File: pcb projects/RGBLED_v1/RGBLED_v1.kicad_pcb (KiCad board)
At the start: 2 copper layers, 63 x 43 mm, 26 parts, among them CN1 USB_B_Micro, CN2 Conn_01x03_Pin, J1 Conn_02x02_Odd_Even, SW1 SW_MEC_5E, U1 STM32F091RBTx, U3 LM1117T-3.3, Y1 32.768kHz

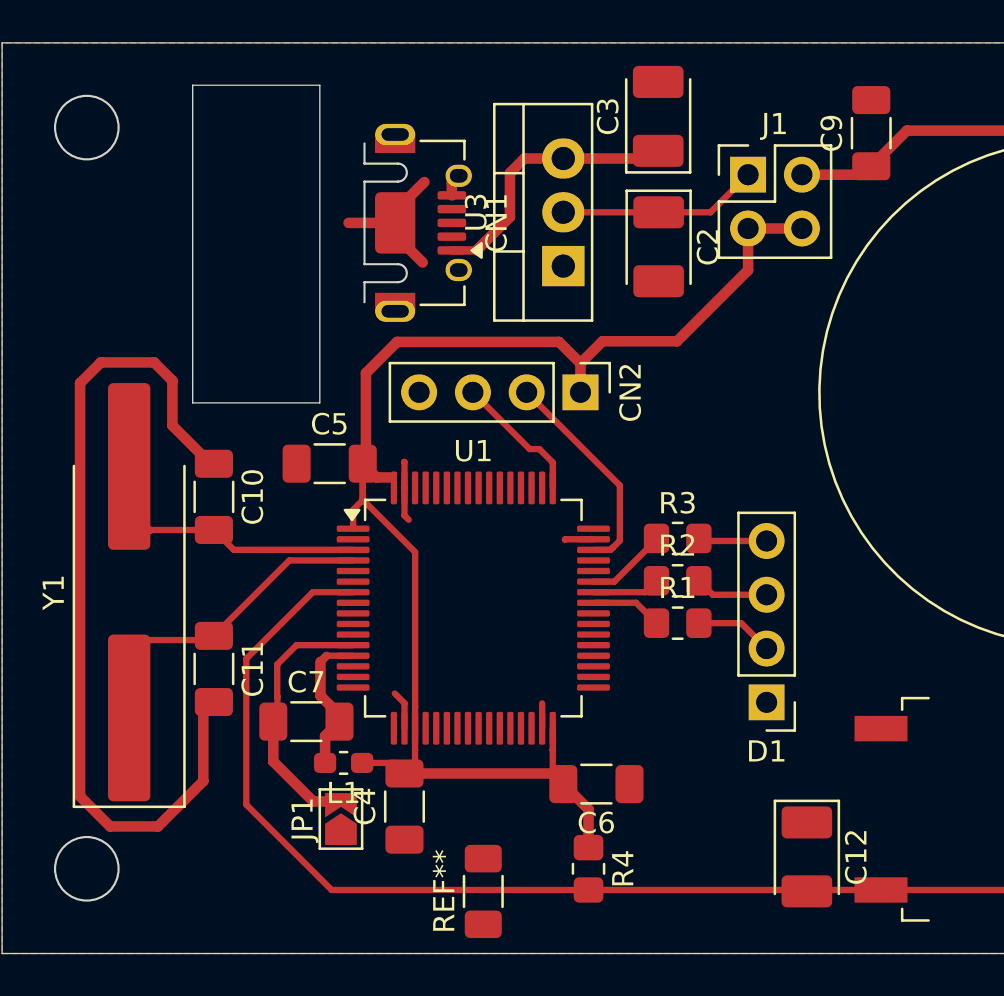
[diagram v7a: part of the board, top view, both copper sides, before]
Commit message: D1 sch fix, stab fix, gnd zone fixed, started verification and BOM
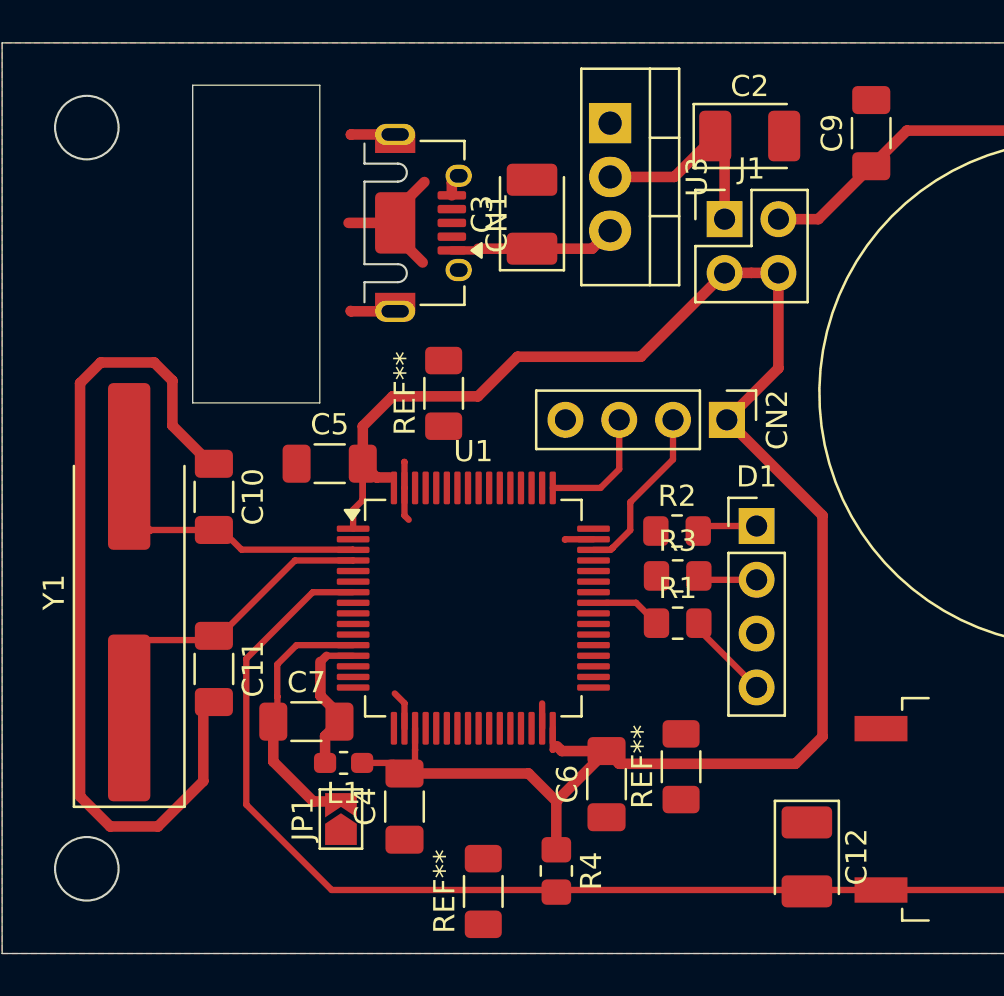
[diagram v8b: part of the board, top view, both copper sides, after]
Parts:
- added REF**: R_1206_3216Metric_Pad1.30x1.75mm_HandSolder, Resistor_SMD:R_1206_3216Metric_Pad1.30x1.75mm_HandSolder, F.Cu at (0.56, 12.7)
- added REF**: R_1206_3216Metric_Pad1.30x1.75mm_HandSolder, Resistor_SMD:R_1206_3216Metric_Pad1.30x1.75mm_HandSolder, F.Cu at (-10.7, -4.95)
- moved D1 8.34 mm to (4.13, 1.31), turned to 0 degrees
- moved C3 7.54 mm to (-6.48, -13.4)
- moved U3 7.10 mm to (-2.79, -17.7), turned to -90 degrees
- moved CN2 7.03 mm to (2.72, -3.70)
- moved C2 6.77 mm to (3.80, -17.1), turned to 0 degrees
- moved J1 2.37 mm to (2.62, -13.2)
- moved R2 2.35 mm to (0.37, 1.55)
- moved R3 1.77 mm to (0.40, 3.67)
- moved R4 1.52 mm to (-5.33, 17.6)
- moved C6 0.48 mm to (-2.96, 13.5), turned to 90 degrees
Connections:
- net Net-(U1-PC14) renamed /Y1+
- net Net-(U1-PC15) renamed /Y1-
- D1 pad 1: GND -> Net-(D1-K)
- D1 pad 2: Net-(D1-RK) -> Net-(D1-RA)
- D1 pad 3: Net-(D1-GK) -> GND
- D1 pad 4: Net-(D1-BK) -> Net-(D1-BA)
- R1 pad 2: Net-(D1-RK) -> Net-(D1-BA)
- R2 pad 2: Net-(D1-GK) -> Net-(D1-K)
- R3 pad 2: Net-(D1-BK) -> Net-(D1-RA)
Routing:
- net +3.3V: track 68.0 -> 88.2 mm
- net +5V: track 13.0 -> 7.74 mm
- net Net-(U1-PA10): track 4.26 -> 0.00 mm
- net GND: track 56.1 -> 60.3 mm
- net Net-(D1-BA): track 0.00 -> 4.16 mm
- net /Y1+: track 16.4 -> 12.4 mm
- net Net-(D1-RK): track 3.70 -> 0.00 mm
- net Net-(D1-GK): track 3.47 -> 0.00 mm
- net Net-(D1-BK): track 3.25 -> 0.00 mm
- net Net-(U1-PA9): track 3.20 -> 0.00 mm
- net Net-(D1-K): track 0.00 -> 2.86 mm
- net Net-(D1-RA): track 0.00 -> 2.80 mm
- net /TCK: track 10.3 -> 8.17 mm
- net Net-(BT1-+): track 13.6 -> 15.6 mm
- net /Y1-: track 16.6 -> 15.4 mm
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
